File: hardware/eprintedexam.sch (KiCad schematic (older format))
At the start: 18 parts, among them J1 Conn_01x04, J2 Conn_01x08, SW1 SW_Push, SW2 SW_Push, U1 ESP-12F

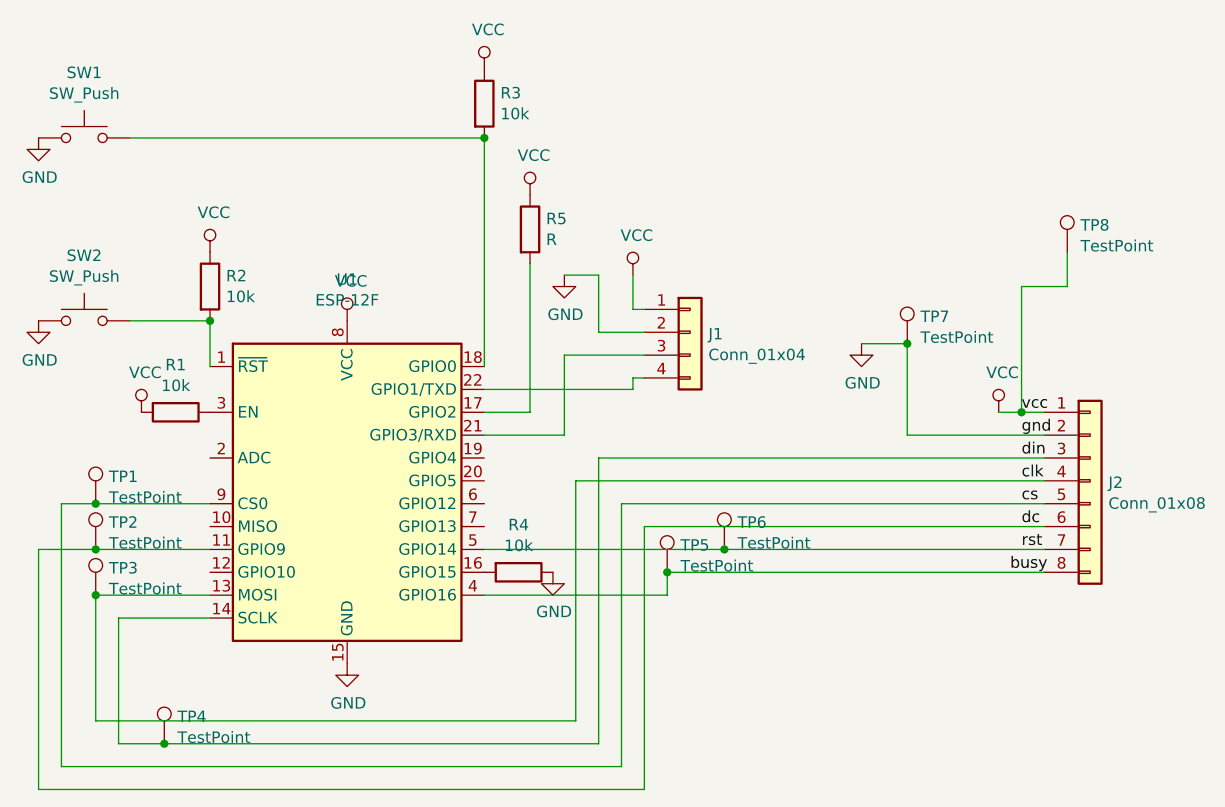
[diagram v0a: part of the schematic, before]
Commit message: updated hardware diagram and added woking epd4in2b_v2 driver
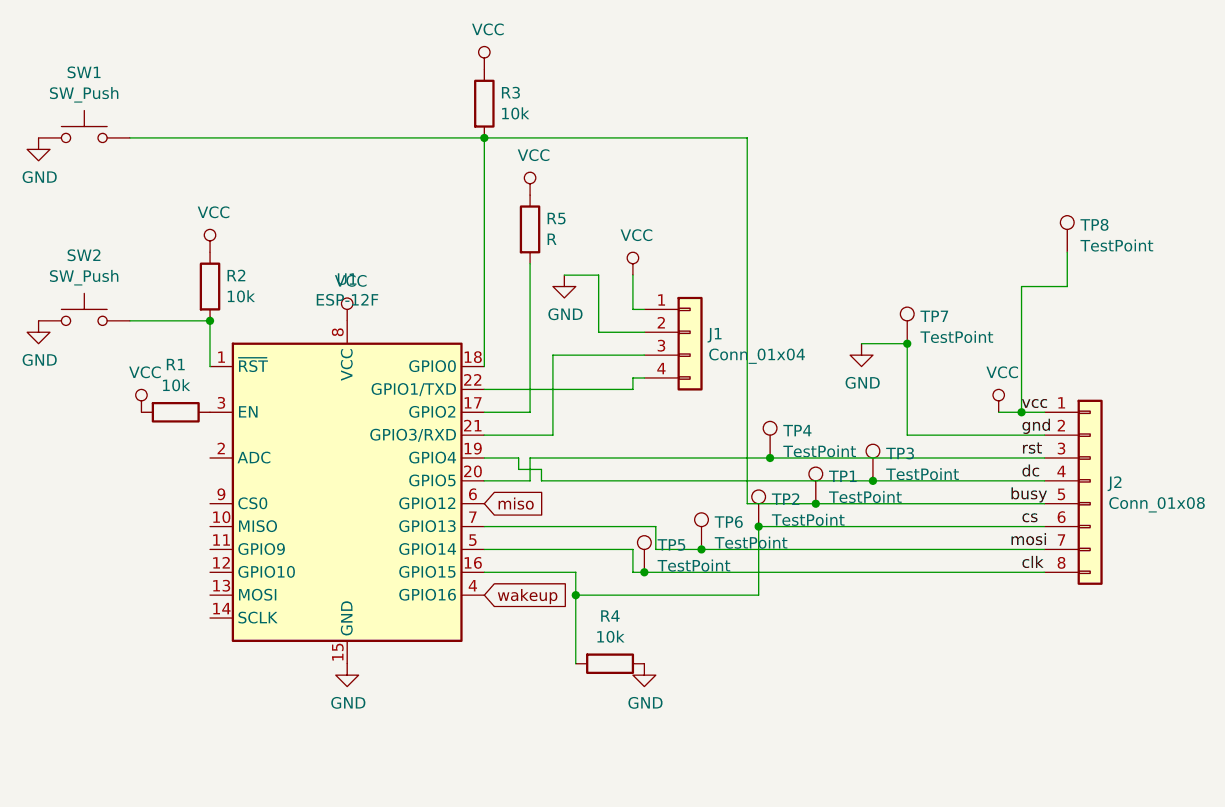
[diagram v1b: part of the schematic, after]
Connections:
- net busy: now also J2.5 (Pin_5), R3.2, SW1.2, TP1.1, U1.18 (GPIO0); no longer J2.8 (Pin_8), TP5.1, U1.4 (GPIO16)
- net clk: now also J2.8 (Pin_8), TP5.1, U1.5 (GPIO14); no longer J2.4 (Pin_4), TP3.1, U1.13 (MOSI)
- net cs: now also J2.6 (Pin_6), R4.2, TP2.1, U1.16 (GPIO15); no longer J2.5 (Pin_5), TP1.1, U1.9 (CS0)
- net dc: now also J2.4 (Pin_4), TP3.1, U1.19 (GPIO4); no longer J2.6 (Pin_6), TP2.1, U1.11 (GPIO9)
- net rst: now also J2.3 (Pin_3), TP4.1, U1.20 (GPIO5); no longer J2.7 (Pin_7), TP6.1, U1.5 (GPIO14)
- net miso: now reaches U1.6 (GPIO12)
- net mosi: now reaches U1.7 (GPIO13)
- net mosi: now also J2.7 (Pin_7), TP6.1
- removed net din: J2.3 (Pin_3), TP4.1, U1.14 (SCLK)
- new net wakeup: U1.4 (GPIO16)
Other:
- moved on the sheet: R4, TP1, TP2, TP3, TP4, TP5, TP6
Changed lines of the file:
@@
 Wire Wire Line
 	4800 2100 4800 2500
-Wire Wire Line
-	3350 3750 1250 3750
-Wire Wire Line
-	1250 3750 1250 3200
-Wire Wire Line
-	1250 3200 1750 3200
-Wire Wire Line
-	3450 3850 1550 3850
-Wire Wire Line
-	1350 3850 1350 3300
-Wire Wire Line
-	1350 3300 1750 3300
-Wire Wire Line
-	5400 2900 3650 2900
-Wire Wire Line
-	3650 2900 3650 4050
-Wire Wire Line
-	3650 4050 1000 4050
-Wire Wire Line
-	1000 4050 1000 3000
-Wire Wire Line
-	1000 3000 1250 3000
-Wire Wire Line
-	5400 3000 4000 3000
 $Comp
 L power:GND #PWR06
@@
 	1    0    0    -1
 $EndComp
-$Comp
-L power:GND #PWR08
-U 1 1 627DFF62
-P 3300 1800
-F 0 "#PWR08" H 3300 1550 50  0001 C CNN
-F 1 "GND" H 3305 1627 50  0000 C CNN
-F 2 "" H 3300 1800 50  0001 C CNN
-F 3 "" H 3300 1800 50  0001 C CNN
-	1    3300 1800
-	1    0    0    -1
-$EndComp
-Wire Wire Line
-	2950 2500 3300 2500
+Wire Wire Line
+	2950 2500 3250 2500
 Wire Wire Line
 	1400 2000 1750 2000
@@
 	1    0    0    -1
 $EndComp
-Wire Wire Line
-	1100 2800 1100 3950
-Wire Wire Line
-	1100 3950 3550 3950
-Wire Wire Line
-	3550 3950 3550 2800
-Wire Wire Line
-	3550 2800 5400 2800
-Wire Wire Line
-	1100 2800 1250 2800
 $Comp
 L Connector_Generic:Conn_01x04 J1
@@
 $EndComp
 Wire Wire Line
-	3300 2150 3650 2150
-Wire Wire Line
-	3300 2150 3300 2500
-Wire Wire Line
 	3600 2300 3600 2250
 Wire Wire Line
@@
 L Connector:TestPoint TP4
 U 1 1 62819007
-P 1550 3850
-F 0 "TP4" H 1608 3968 50  0000 L CNN
-F 1 "TestPoint" H 1608 3877 50  0000 L CNN
-F 2 "TestPoint:TestPoint_Pad_D1.5mm" H 1750 3850 50  0001 C CNN
-F 3 "~" H 1750 3850 50  0001 C CNN
-	1    1550 3850
-	1    0    0    -1
-$EndComp
-$Comp
-L Connector:TestPoint TP3
-U 1 1 62819A95
-P 1250 3200
-F 0 "TP3" H 1308 3318 50  0000 L CNN
-F 1 "TestPoint" H 1308 3227 50  0000 L CNN
-F 2 "TestPoint:TestPoint_Pad_D1.5mm" H 1450 3200 50  0001 C CNN
-F 3 "~" H 1450 3200 50  0001 C CNN
-	1    1250 3200
+P 4200 2600
+F 0 "TP4" H 4258 2718 50  0000 L CNN
+F 1 "TestPoint" H 4258 2627 50  0000 L CNN
+F 2 "TestPoint:TestPoint_Pad_D1.5mm" H 4400 2600 50  0001 C CNN
+F 3 "~" H 4400 2600 50  0001 C CNN
+	1    4200 2600
 	1    0    0    -1
 $EndComp
@@
 L Connector:TestPoint TP2
 U 1 1 6281A574
-P 1250 3000
-F 0 "TP2" H 1308 3118 50  0000 L CNN
-F 1 "TestPoint" H 1308 3027 50  0000 L CNN
-F 2 "TestPoint:TestPoint_Pad_D1.5mm" H 1450 3000 50  0001 C CNN
-F 3 "~" H 1450 3000 50  0001 C CNN
-	1    1250 3000
+P 4150 2900
+F 0 "TP2" H 4208 3018 50  0000 L CNN
+F 1 "TestPoint" H 4208 2927 50  0000 L CNN
+F 2 "TestPoint:TestPoint_Pad_D1.5mm" H 4350 2900 50  0001 C CNN
+F 3 "~" H 4350 2900 50  0001 C CNN
+	1    4150 2900
 	1    0    0    -1
 $EndComp
@@
 L Connector:TestPoint TP1
 U 1 1 6281AFD3
-P 1250 2800
-F 0 "TP1" H 1308 2918 50  0000 L CNN
-F 1 "TestPoint" H 1308 2827 50  0000 L CNN
-F 2 "TestPoint:TestPoint_Pad_D1.5mm" H 1450 2800 50  0001 C CNN
-F 3 "~" H 1450 2800 50  0001 C CNN
-	1    1250 2800
+P 4400 2800
+F 0 "TP1" H 4458 2918 50  0000 L CNN
+F 1 "TestPoint" H 4458 2827 50  0000 L CNN
+F 2 "TestPoint:TestPoint_Pad_D1.5mm" H 4600 2800 50  0001 C CNN
+F 3 "~" H 4600 2800 50  0001 C CNN
+	1    4400 2800
 	1    0    0    -1
 $EndComp
@@
 L Connector:TestPoint TP5
 U 1 1 6281BB33
-P 3750 3100
-F 0 "TP5" H 3808 3218 50  0000 L CNN
-F 1 "TestPoint" H 3808 3127 50  0000 L CNN
-F 2 "TestPoint:TestPoint_Pad_D1.5mm" H 3950 3100 50  0001 C CNN
-F 3 "~" H 3950 3100 50  0001 C CNN
-	1    3750 3100
+P 3650 3100
+F 0 "TP5" H 3708 3218 50  0000 L CNN
+F 1 "TestPoint" H 3708 3127 50  0000 L CNN
+F 2 "TestPoint:TestPoint_Pad_D1.5mm" H 3850 3100 50  0001 C CNN
+F 3 "~" H 3850 3100 50  0001 C CNN
+	1    3650 3100
 	1    0    0    -1
 $EndComp
@@
 L Connector:TestPoint TP6
 U 1 1 6281C6BA
-P 4000 3000
-F 0 "TP6" H 4058 3118 50  0000 L CNN
-F 1 "TestPoint" H 4058 3027 50  0000 L CNN
-F 2 "TestPoint:TestPoint_Pad_D1.5mm" H 4200 3000 50  0001 C CNN
-F 3 "~" H 4200 3000 50  0001 C CNN
-	1    4000 3000
-	1    0    0    -1
-$EndComp
-Connection ~ 1550 3850
-Wire Wire Line
-	1550 3850 1350 3850
-Connection ~ 1250 3200
-Connection ~ 1250 3000
-Wire Wire Line
-	1250 3000 1750 3000
-Connection ~ 1250 2800
-Wire Wire Line
-	3750 3100 5400 3100
-Connection ~ 4000 3000
-Wire Wire Line
-	2950 3000 4000 3000
+P 3900 3000
+F 0 "TP6" H 3958 3118 50  0000 L CNN
+F 1 "TestPoint" H 3958 3027 50  0000 L CNN
+F 2 "TestPoint:TestPoint_Pad_D1.5mm" H 4100 3000 50  0001 C CNN
+F 3 "~" H 4100 3000 50  0001 C CNN
+	1    3900 3000
+	1    0    0    -1
+$EndComp
 Text Label 5300 2400 0    50   ~ 0
 vcc
 Text Label 5300 2500 0    50   ~ 0
 gnd
+Text Label 5250 3000 0    50   ~ 0
+mosi
+Text Label 5300 3100 0    50   ~ 0
+clk
+Text Label 5300 2900 0    50   ~ 0
+cs
+Text Label 5300 2700 0    50   ~ 0
+dc
 Text Label 5300 2600 0    50   ~ 0
-din
-Text Label 5300 2700 0    50   ~ 0
-clk
-Text Label 5300 2800 0    50   ~ 0
-cs
-Text Label 5300 2900 0    50   ~ 0
-dc
-Text Label 5300 3000 0    50   ~ 0
 rst
-Text Label 5250 3100 0    50   ~ 0
+Text Label 5250 2800 0    50   ~ 0
 busy
-Wire Wire Line
-	3750 3100 3750 3200
-Wire Wire Line
-	3750 3200 2950 3200
-Connection ~ 3750 3100
-Wire Wire Line
-	1250 2800 1750 2800
+$Comp
+L Device:R R4
+U 1 1 6281AA4E
+P 3500 3500
+F 0 "R4" V 3293 3500 50  0000 C CNN
+F 1 "10k" V 3384 3500 50  0000 C CNN
+F 2 "Resistor_SMD:R_1206_3216Metric" V 3430 3500 50  0001 C CNN
+F 3 "~" H 3500 3500 50  0001 C CNN
+	1    3500 3500
+	0    1    1    0
+$EndComp
+$Comp
+L power:GND #PWR0102
+U 1 1 6281CF23
+P 3650 3500
+F 0 "#PWR0102" H 3650 3250 50  0001 C CNN
+F 1 "GND" H 3655 3327 50  0000 C CNN
+F 2 "" H 3650 3500 50  0001 C CNN
+F 3 "" H 3650 3500 50  0001 C CNN
+	1    3650 3500
+	1    0    0    -1
+$EndComp
+$Comp
+L Device:R R5
+U 1 1 6281DBF9
+P 3150 1600
+F 0 "R5" H 3220 1646 50  0000 L CNN
+F 1 "R" H 3220 1555 50  0000 L CNN
+F 2 "Resistor_SMD:R_1206_3216Metric" V 3080 1600 50  0001 C CNN
+F 3 "~" H 3150 1600 50  0001 C CNN
+	1    3150 1600
+	1    0    0    -1
+$EndComp
+Wire Wire Line
+	3150 1750 3150 2400
+Wire Wire Line
+	3150 2400 2950 2400
+$Comp
+L power:VCC #PWR0103
+U 1 1 62821BBF
+P 3150 1450
+F 0 "#PWR0103" H 3150 1300 50  0001 C CNN
+F 1 "VCC" H 3167 1623 50  0000 C CNN
+F 2 "" H 3150 1450 50  0001 C CNN
+F 3 "" H 3150 1450 50  0001 C CNN
+	1    3150 1450
+	1    0    0    -1
+$EndComp
+Wire Wire Line
+	4650 2700 5400 2700
+Wire Wire Line
+	4400 2800 5400 2800
+Wire Wire Line
+	4150 2900 5400 2900
+Wire Wire Line
+	3350 3100 3350 3200
+Wire Wire Line
+	2950 3100 3350 3100
 $Comp
 L RF_Module:ESP-12F U1
@@
 	1    0    0    -1
 $EndComp
-$Comp
-L Device:R R4
-U 1 1 6281AA4E
-P 3100 3100
-F 0 "R4" V 2893 3100 50  0000 C CNN
-F 1 "10k" V 2984 3100 50  0000 C CNN
-F 2 "Resistor_SMD:R_1206_3216Metric" V 3030 3100 50  0001 C CNN
-F 3 "~" H 3100 3100 50  0001 C CNN
-	1    3100 3100
-	0    1    1    0
-$EndComp
-$Comp
-L power:GND #PWR0102
-U 1 1 6281CF23
-P 3250 3100
-F 0 "#PWR0102" H 3250 2850 50  0001 C CNN
-F 1 "GND" H 3255 2927 50  0000 C CNN
-F 2 "" H 3250 3100 50  0001 C CNN
-F 3 "" H 3250 3100 50  0001 C CNN
-	1    3250 3100
-	1    0    0    -1
-$EndComp
-$Comp
-L Device:R R5
-U 1 1 6281DBF9
-P 3150 1600
-F 0 "R5" H 3220 1646 50  0000 L CNN
-F 1 "R" H 3220 1555 50  0000 L CNN
-F 2 "Resistor_SMD:R_1206_3216Metric" V 3080 1600 50  0001 C CNN
-F 3 "~" H 3150 1600 50  0001 C CNN
-	1    3150 1600
-	1    0    0    -1
-$EndComp
-Wire Wire Line
-	3150 1750 3150 2400
-Wire Wire Line
-	3150 2400 2950 2400
-$Comp
-L power:VCC #PWR0103
-U 1 1 62821BBF
-P 3150 1450
-F 0 "#PWR0103" H 3150 1300 50  0001 C CNN
-F 1 "VCC" H 3167 1623 50  0000 C CNN
-F 2 "" H 3150 1450 50  0001 C CNN
-F 3 "" H 3150 1450 50  0001 C CNN
-	1    3150 1450
-	1    0    0    -1
-$EndComp
-Wire Wire Line
-	3450 2600 5400 2600
-Wire Wire Line
-	3450 2600 3450 3850
-Wire Wire Line
-	3350 2700 5400 2700
-Wire Wire Line
-	3350 2700 3350 3750
+Wire Wire Line
+	3250 2150 3250 2500
+Wire Wire Line
+	3250 2150 3650 2150
+Wire Wire Line
+	3700 3000 3900 3000
+Connection ~ 3900 3000
+Wire Wire Line
+	3900 3000 5400 3000
+Wire Wire Line
+	3600 3100 3600 3000
+Wire Wire Line
+	3600 3000 2950 3000
+Wire Wire Line
+	3600 3100 3650 3100
+Connection ~ 3650 3100
+Wire Wire Line
+	3650 3100 5400 3100
+Wire Wire Line
+	3700 3000 3700 2900
+Wire Wire Line
+	3700 2900 2950 2900
+Connection ~ 4150 2900
+Wire Wire Line
+	3350 3200 4150 3200
+Wire Wire Line
+	4150 3200 4150 2900
+Connection ~ 3350 3200
+Wire Wire Line
+	3350 3200 3350 3500
+$Comp
+L power:GND #PWR0104
+U 1 1 62842628
+P 3300 1800
+F 0 "#PWR0104" H 3300 1550 50  0001 C CNN
+F 1 "GND" H 3305 1627 50  0000 C CNN
+F 2 "" H 3300 1800 50  0001 C CNN
+F 3 "" H 3300 1800 50  0001 C CNN
+	1    3300 1800
+	1    0    0    -1
+$EndComp
+$Comp
+L Connector:TestPoint TP3
+U 1 1 62819A95
+P 4650 2700
+F 0 "TP3" H 4708 2818 50  0000 L CNN
+F 1 "TestPoint" H 4708 2727 50  0000 L CNN
+F 2 "TestPoint:TestPoint_Pad_D1.5mm" H 4850 2700 50  0001 C CNN
+F 3 "~" H 4850 2700 50  0001 C CNN
+	1    4650 2700
+	1    0    0    -1
+$EndComp
+Text GLabel 2950 3200 2    50   Input ~ 0
+wakeup
+Text GLabel 2950 2800 2    50   Input ~ 0
+miso
+Wire Wire Line
+	4100 1200 2950 1200
+Wire Wire Line
+	4200 2600 5400 2600
+Wire Wire Line
+	4400 2800 4100 2800
+Wire Wire Line
+	4100 2800 4100 1200
+Connection ~ 4400 2800
+Wire Wire Line
+	4200 2600 3150 2600
+Wire Wire Line
+	3150 2600 3150 2700
+Wire Wire Line
+	3150 2700 2950 2700
+Connection ~ 4200 2600
+Wire Wire Line
+	2950 2600 3100 2600
+Wire Wire Line
+	3100 2600 3100 2650
+Wire Wire Line
+	3100 2650 3200 2650
+Wire Wire Line
+	3200 2650 3200 2700
+Wire Wire Line
+	3200 2700 4650 2700
+Connection ~ 4650 2700
 $EndSCHEMATC

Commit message: mayor hardware revision
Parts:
- removed R2: 10k, Resistor_SMD:R_1206_3216Metric, symbol Device:R
- removed R5: R, Resistor_SMD:R_1206_3216Metric, symbol Device:R
- removed TP7, TP8: TestPoint, TestPoint:TestPoint_Pad_D1.5mm, symbol Connector:TestPoint
- added BT1: Battery_Cell, Battery:BatteryHolder_MPD_BH-18650-PC2, symbol Device:Battery_Cell
- added C1, C2, C3, C4, C5, C7: 100n, Capacitor_SMD:C_1206_3216Metric, symbol Device:C
- added C6: 10n, Capacitor_SMD:C_1206_3216Metric, symbol Device:C
- added D1: D, Diode_THT:D_DO-35_SOD27_P10.16mm_Horizontal, symbol Device:D
- added H1, H2, H3, H4: MountingHole, MountingHole:MountingHole_3mm, symbol Mechanical:MountingHole
- added Q1, Q2, Q3, Q4, Q5: 2N7002, Package_TO_SOT_SMD:SOT-23, symbol Transistor_FET:2N7002
- added Q6: AO3401A, Package_TO_SOT_SMD:SOT-23, symbol Transistor_FET:AO3401A
- added R10, R11: 33k, Resistor_SMD:R_1206_3216Metric, symbol Device:R
- added R12, R15, R16, R18, R8, R9: 10k, Resistor_SMD:R_1206_3216Metric, symbol Device:R
- added R13: 330, Resistor_SMD:R_1206_3216Metric, symbol Device:R
- added R14: 22k, Resistor_SMD:R_1206_3216Metric, symbol Device:R
- added R17: 560k, Resistor_SMD:R_1206_3216Metric, symbol Device:R
- added R6, R7: 1k, Resistor_SMD:R_1206_3216Metric, symbol Device:R
- added SW3, SW4: SW_Push, Button_Switch_SMD:SW_SPST_TL3342, symbol Switch:SW_Push
- added U1: AP1117-33, Package_TO_SOT_SMD:SOT-223-3_TabPin2, symbol Regulator_Linear:AP1117-33
- renumbered R1 to R2, SW2 to SW1, SW1 to SW2, TP2 to TP1, TP5 to TP2, TP6 to TP3, TP1 to TP4, TP3 to TP5, TP4 to TP6, U1 to U2
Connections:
- net wakeup is gone; now on net nrst: U2.4 (GPIO16)
- net GND: now also BT1.2 (-), C1.2, C2.1, C3.2, C4.2, C7.2, Q2.2 (S), Q3.2 (S), Q4.3 (D), Q5.2 (S), R13.2, R15.2, R18.1, SW3.1, SW4.1, U1.1 (GND)
- net VCC: now also C2.2, D1.1 (K), Q6.3 (D), R10.2, R11.2, R12.1, R14.1, R17.1, R8.2, R9.2, U1.2 (VO)
- net nrst: now reaches SW1.2, U2.1 (~RST)
- net nrst: now also C1.1, C5.2, D1.2 (A), Q4.2 (S), R12.2
- net prv: now reaches U2.17 (GPIO2)
- net prv: now also C4.1, Q2.1 (G), R7.1, R9.1
- net nxt: now reaches J1.3 (Pin_3), U2.21 (GPIO3/RXD)
- net nxt: now also C3.1, Q1.1 (G), R6.1, R8.1
- net busy renamed spi-busy,flash
- net spi-busy,flash: now also J2.8 (Pin_8), TP6.1; no longer J2.5 (Pin_5), TP4.1
- net clk renamed spi-clk
- net spi-clk: now also J2.4 (Pin_4); no longer J2.8 (Pin_8)
- net cs renamed spi-cs
- net spi-cs: now also J2.5 (Pin_5), TP3.1; no longer J2.6 (Pin_6), TP1.1
- removed net dc: J2.4 (Pin_4), TP5.1, U2.19 (GPIO4)
- net miso renamed spi-miso
- removed net mosi: J2.7 (Pin_7), TP3.1, U2.7 (GPIO13)
- removed net rst: J2.3 (Pin_3), TP6.1, U2.20 (GPIO5)
- new net: BT1.1 (+), U1.3 (VI)
- new net: R6.2, SW3.2
- new net: C7.1, Q6.1 (G), R16.1
- new net: Q1.2 (S), Q2.3 (D)
- new net: Q1.3 (D), Q3.1 (G), R10.1
- new net: R7.2, SW4.2
- new net: C6.2, Q4.1 (G), R13.1
- new net: C6.1, Q5.3 (D), R17.2
- new net nxt+prv: C5.1, Q3.3 (D), Q5.1 (G), R11.1, R14.2
- new net spi-dc: J2.6 (Pin_6), TP4.1, U2.19 (GPIO4)
- new net spi-mosi: J2.3 (Pin_3), TP1.1, U2.7 (GPIO13)
- new net spi-nrst: J2.7 (Pin_7), Q6.2 (S), R18.2
- new net spi-rst: R15.1, R16.2, TP5.1, U2.20 (GPIO5)
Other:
- note added: "display connector"
- note added: "flash button"
- note added: "gpio2 pullup in NOR gate component"
- note added: "logic NOR of singals prv and nxt"
- note added: "main esp8266 wiring"
- note added: "mounting holes"
- note added: "not gate for spi-rst singal"
- note added: "nrts pullup in monostable component"
- note added: "single pulse monostable\nfor reset pulse from nxt+prv signal"
- note added: "test points for display"
- note added: "voltage regulation"
- moved on the sheet: J1, J2, R2, R3, R4, SW1, SW2, TP1, TP2, TP3, TP4, TP5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

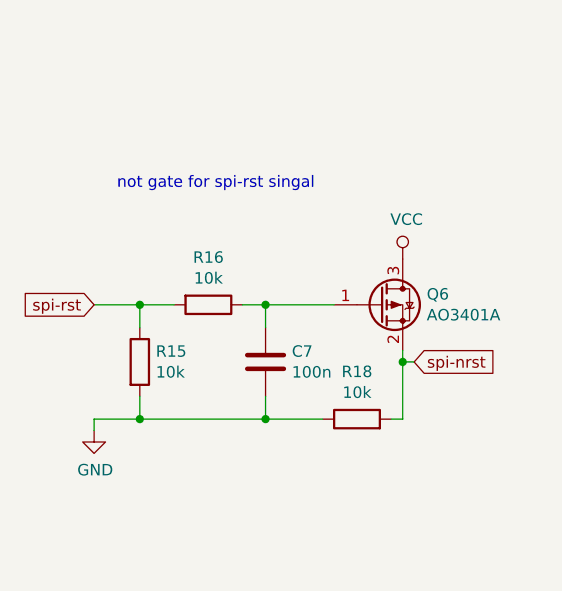
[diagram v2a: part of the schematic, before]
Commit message: changed p-mosfet for n-mosfet in signal inversor
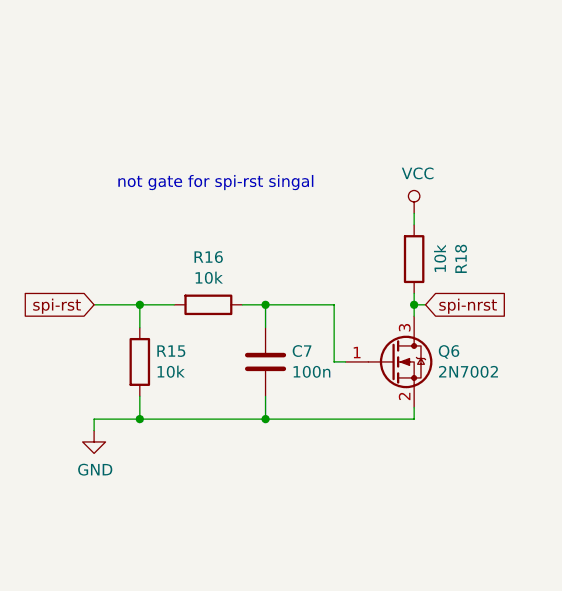
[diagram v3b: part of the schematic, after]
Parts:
- removed Q6: AO3401A, Package_TO_SOT_SMD:SOT-23, symbol Transistor_FET:AO3401A
- added Q6: 2N7002, Package_TO_SOT_SMD:SOT-23, symbol Transistor_FET:2N7002
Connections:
- net GND: now also Q6.2 (S); no longer R18.1
- net VCC: now also R18.2
- net spi-nrst: now also R18.1, Q6.3 (D); no longer R18.2
- net at C7.1, R16.1: now also Q6.1 (G)
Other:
- moved on the sheet: R18
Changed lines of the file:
@@
 Wire Wire Line
 	8950 5000 9150 5000
-$Comp
-L Transistor_FET:AO3401A Q6
-U 1 1 62DE7C17
-P 10200 5000
-F 0 "Q6" H 10405 5046 50  0000 L CNN
-F 1 "AO3401A" H 10405 4955 50  0000 L CNN
-F 2 "Package_TO_SOT_SMD:SOT-23" H 10400 4925 50  0001 L CIN
-F 3 "http://www.aosmd.com/pdfs/datasheet/AO3401A.pdf" H 10200 5000 50  0001 L CNN
-	1    10200 5000
-	1    0    0    -1
-$EndComp
-Wire Wire Line
-	10300 5250 10300 5500
-Connection ~ 10300 5250
-Wire Wire Line
-	10300 5250 10350 5250
-Wire Wire Line
-	10300 5500 10250 5500
-Wire Wire Line
-	10300 5200 10300 5250
-Wire Wire Line
-	9700 5500 9950 5500
 Wire Wire Line
 	9700 5000 10000 5000
@@
 L Device:R R18
 U 1 1 62DE7C00
-P 10100 5500
-F 0 "R18" V 10307 5500 50  0000 C CNN
-F 1 "10k" V 10216 5500 50  0000 C CNN
-F 2 "Resistor_SMD:R_1206_3216Metric" V 10030 5500 50  0001 C CNN
-F 3 "~" H 10100 5500 50  0001 C CNN
-	1    10100 5500
-	0    -1   -1   0
+P 10350 4800
+F 0 "R18" V 10557 4800 50  0000 C CNN
+F 1 "10k" V 10466 4800 50  0000 C CNN
+F 2 "Resistor_SMD:R_1206_3216Metric" V 10280 4800 50  0001 C CNN
+F 3 "~" H 10350 4800 50  0001 C CNN
+	1    10350 4800
+	1    0    0    1
 $EndComp
 $Comp
 L power:VCC #PWR027
 U 1 1 62DE7BFA
-P 10300 4800
-F 0 "#PWR027" H 10300 4650 50  0001 C CNN
-F 1 "VCC" H 10317 4973 50  0000 C CNN
-F 2 "" H 10300 4800 50  0001 C CNN
-F 3 "" H 10300 4800 50  0001 C CNN
-	1    10300 4800
+P 10350 4600
+F 0 "#PWR027" H 10350 4450 50  0001 C CNN
+F 1 "VCC" H 10367 4773 50  0000 C CNN
+F 2 "" H 10350 4600 50  0001 C CNN
+F 3 "" H 10350 4600 50  0001 C CNN
+	1    10350 4600
 	1    0    0    -1
 $EndComp
@@
 	1    0    0    -1
 $EndComp
-Text GLabel 10350 5250 2    50   Input ~ 0
+Text GLabel 10400 5000 2    50   Input ~ 0
 spi-nrst
 Text GLabel 8950 5000 0    50   Input ~ 0
@@
 	3900 5650 4200 5650
 Connection ~ 3900 5650
+$Comp
+L Transistor_FET:2N7002 Q6
+U 1 1 629D5A7E
+P 10250 5250
+F 0 "Q6" H 10454 5296 50  0000 L CNN
+F 1 "2N7002" H 10454 5205 50  0000 L CNN
+F 2 "Package_TO_SOT_SMD:SOT-23" H 10450 5175 50  0001 L CIN
+F 3 "https://www.fairchildsemi.com/datasheets/2N/2N7002.pdf" H 10250 5250 50  0001 L CNN
+	1    10250 5250
+	1    0    0    -1
+$EndComp
+Wire Wire Line
+	10350 5500 10350 5450
+Wire Wire Line
+	9700 5500 10350 5500
+Wire Wire Line
+	10000 5000 10000 5250
+Wire Wire Line
+	10000 5250 10050 5250
+Wire Wire Line
+	10350 4600 10350 4650
+Wire Wire Line
+	10350 4950 10350 5000
+Wire Wire Line
+	10350 5000 10400 5000
+Connection ~ 10350 5000
+Wire Wire Line
+	10350 5000 10350 5050
 $EndSCHEMATC
